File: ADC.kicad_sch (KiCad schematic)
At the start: 32 parts, among them U107 ADR4540, U111 ADA4841-1, U97 AD7768

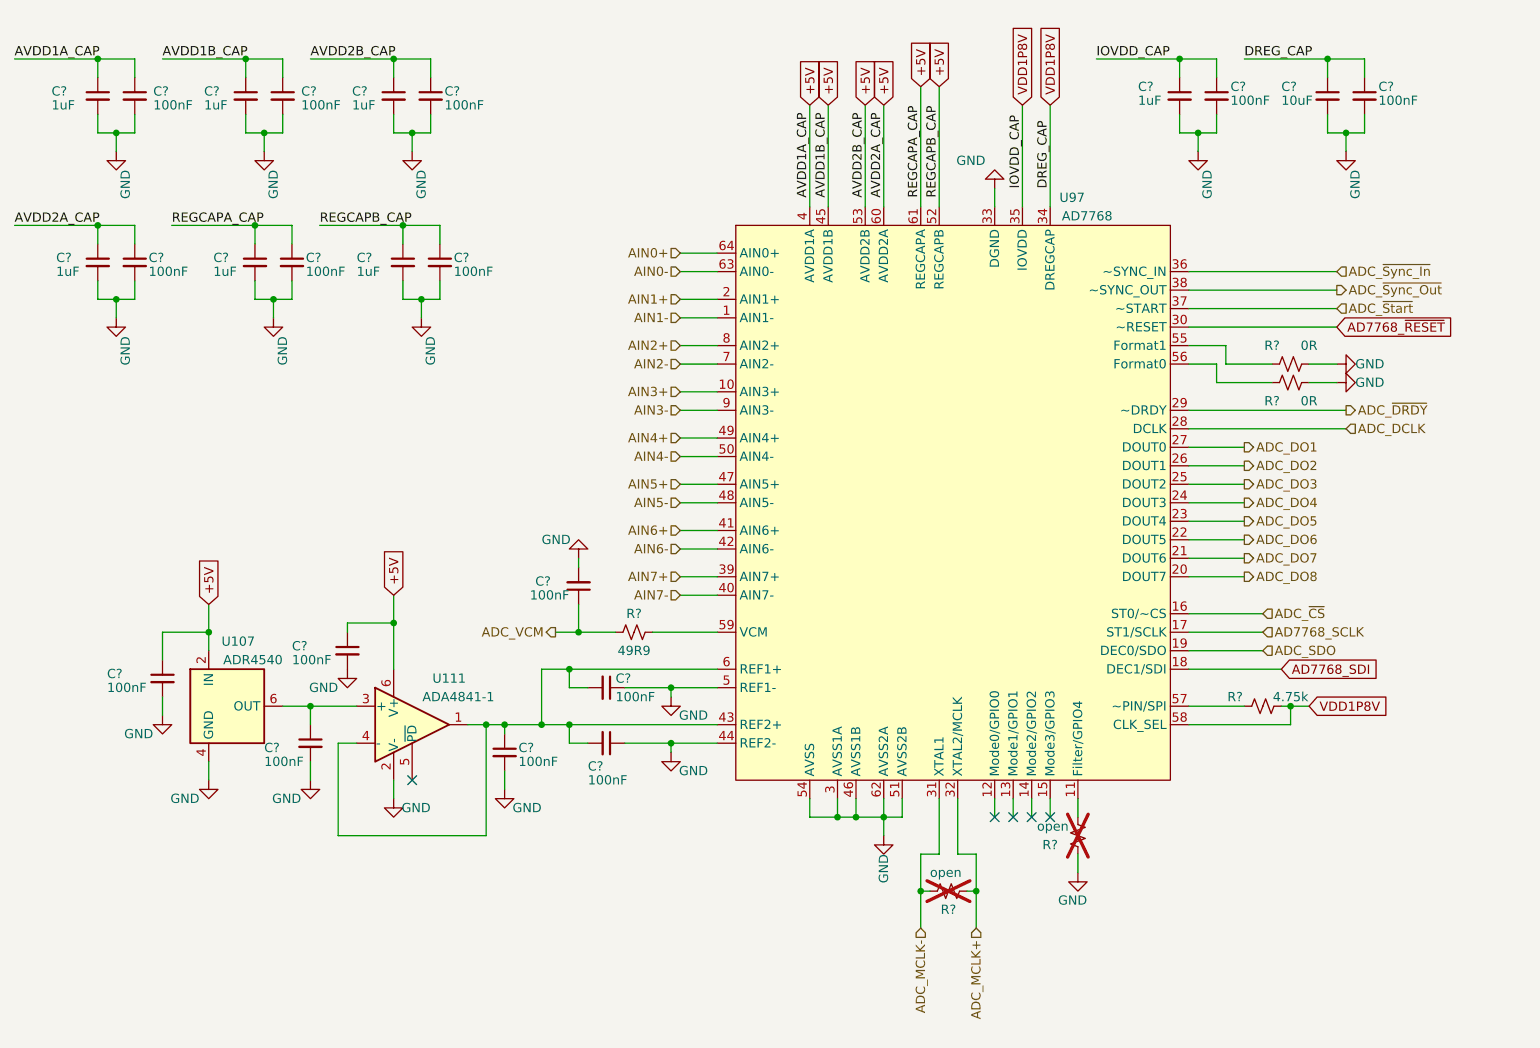
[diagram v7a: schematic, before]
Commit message: Update to Schematics; initial PCB commit
-Updated Power, Housekeeping, and ADCs sheets.
-Remapped FMC pins
-Initial board layout commit
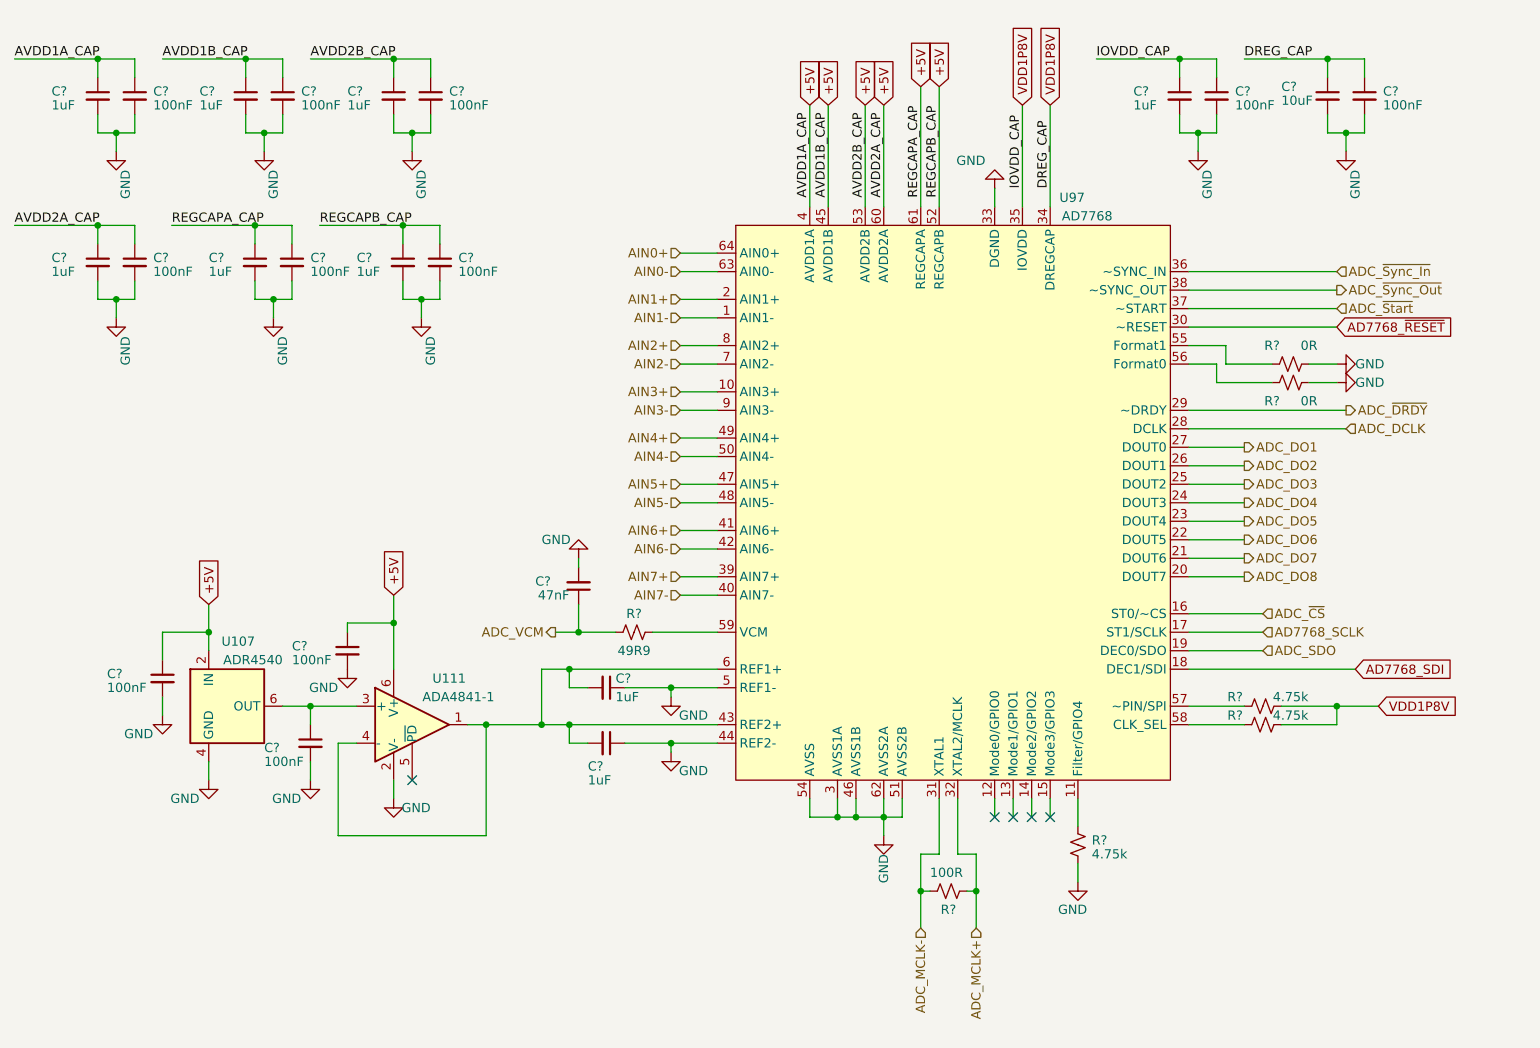
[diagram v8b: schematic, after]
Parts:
- removed C? (x8): 100nF, Capacitor_SMD:C_0603_1608Metric, symbol Device:C_Small
- removed C? (x6): 1uF, Capacitor_SMD:C_0603_1608Metric, symbol Device:C_Small
- removed R?: open, Resistor_SMD:R_0603_1608Metric, symbol Device:R_Small_US
- added C? (x7): 100nF, Capacitor_SMD:C_0402_1005Metric, symbol Device:C_Small
- added C? (x6): 1uF, Capacitor_SMD:C_0402_1005Metric, symbol Device:C_Small
- added R? (x2): 4.75k, Resistor_SMD:R_0402_1005Metric, symbol Device:R_Small_US
- C? (x5): footprint Capacitor_SMD:C_0603_1608Metric -> Capacitor_SMD:C_0402_1005Metric
- C?: value 100nF -> 47nF; footprint Capacitor_SMD:C_0603_1608Metric -> Capacitor_SMD:C_0402_1005Metric; MPN CL10B104KB8NNWC -> (none)
- C? (x2): value 100nF -> 1uF; footprint Capacitor_SMD:C_0603_1608Metric -> Capacitor_SMD:C_0402_1005Metric; MPN CL10B104KB8NNWC -> (none)
- R?: value open -> 100R; footprint Resistor_SMD:R_0603_1608Metric -> Resistor_SMD:R_0402_1005Metric; now fitted
- R? (x3): footprint Resistor_SMD:R_0603_1608Metric -> Resistor_SMD:R_0402_1005Metric
- R?: footprint (none) -> Resistor_SMD:R_0402_1005Metric
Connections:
- net +5V: now also C?.1, C?.1, C?.1, C?.1, C?.1, C?.1, C?.1, C?.1, C?.1, C?.1
- net GND: now also C?.2, C?.2, C?.2, C?.2, C?.2, C?.2, C?.2, C?.2, C?.2, C?.2, C?.2, C?.2, C?.2, R?.2
- net VDD1P8V: now also C?.1, C?.1, C?.1, R?.1; no longer U97.58 (CLK_SEL)
- net at U97.11 (Filter/GPIO4): now also R?.1
- new net: R?.2, U97.58 (CLK_SEL)
